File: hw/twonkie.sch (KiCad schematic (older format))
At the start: 55 parts, among them J1 USB4151, J2 690-024-294T331, J3 629105150521, Q1 BSD840N, Q2 BSD840N, Q3 BSD840N, SW1 EVQ-P7M01P, U1 INA260, U2 INA260, U3 MIC5504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

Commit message: Add back bootloader selection via USB_ID
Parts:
- added Q4: BSD840N, Package_TO_SOT_SMD:SOT-363_SC-70-6, symbol Transistor_FET:FDG6335N
- added R27: 35k7, Resistor_SMD:R_0402_1005Metric_Pad0.72x0.64mm_HandSolder, symbol Device:R
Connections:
- net +3V3: now also R1.1, R27.1; no longer R24.1
- net BOOT: now also R1.2, Q4.1 (S); no longer R1.1, SW1.2
- net GND: now also R24.2, Q4.6 (D); no longer R1.2
- net USB_B_ID: now reaches J3.4 (ID)
- net USB_B_ID: now also SW1.1, Q4.2 (G), R27.2
- new net: R24.1, SW1.2
- no-connect marks 7 -> 6
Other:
- note added: "Bootloader mode"
- note added: "Use A-to-A cable plugged into\nOTG adapter for bootloader mode,\nor use normal Micro-B cable and\nhold SW1 while plugging."
- moved on the sheet: R24
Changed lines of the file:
@@
-$EndComp
-$Comp
-L Switch:SW_Push SW1
-U 1 1 5FAB092D
-P 7500 3200
-F 0 "SW1" H 7500 3400 50  0000 C CNN
-F 1 "EVQ-P7M01P" H 7500 3100 50  0000 C CNN
-F 2 "Button_Switch_SMD:SW_SPST_EVQP7C" H 7500 3500 50  0001 C CNN
-F 3 "http://www.apem.com/int/index.php?controller=attachment&id_attachment=1371" H 7500 3500 50  0001 C CNN
-F 4 "P16770CT-ND" H 7500 3200 50  0001 C CNN "DigiKey P/N"
-F 5 "Panasonic" H 7500 3200 50  0001 C CNN "Manufacturer"
-F 6 "EVQ-P7M01P" H 7500 3200 50  0001 C CNN "Mfg P/N"
-	1    7500 3200
-	-1   0    0    -1
 $EndComp
 $Comp
@@
 	0    -1   -1   0
 $EndComp
-$Comp
-L power:GND #PWR0124
-U 1 1 5FE51FD2
-P 7100 4250
-F 0 "#PWR0124" H 7100 4000 50  0001 C CNN
-F 1 "GND" H 7105 4077 50  0000 C CNN
-F 2 "" H 7100 4250 50  0001 C CNN
-F 3 "" H 7100 4250 50  0001 C CNN
-	1    7100 4250
-	-1   0    0    -1
-$EndComp
-Wire Wire Line
-	7100 3950 8400 3950
-Wire Wire Line
-	7300 3200 7100 3200
-$Comp
-L power:+3V3 #PWR0125
-U 1 1 5FE52452
-P 7850 2900
-F 0 "#PWR0125" H 7850 2750 50  0001 C CNN
-F 1 "+3V3" H 7865 3073 50  0000 C CNN
-F 2 "" H 7850 2900 50  0001 C CNN
-F 3 "" H 7850 2900 50  0001 C CNN
-	1    7850 2900
-	1    0    0    -1
-$EndComp
-$Comp
-L Device:R R1
-U 1 1 5FE52997
-P 7100 4100
-F 0 "R1" H 7170 4146 50  0000 L CNN
-F 1 "35k7" H 7170 4055 50  0000 L CNN
-F 2 "Resistor_SMD:R_0402_1005Metric_Pad0.72x0.64mm_HandSolder" V 7030 4100 50  0001 C CNN
-F 3 "~" H 7100 4100 50  0001 C CNN
-F 4 "311-35.7KLRCT-ND" H 7100 4100 50  0001 C CNN "DigiKey P/N"
-F 5 "RC0402FR-0735K7L" H 7100 4100 50  0001 C CNN "Mfg P/N"
-F 6 "Yageo" H 7100 4100 50  0001 C CNN "Manufacturer"
-	1    7100 4100
-	1    0    0    -1
-$EndComp
 Wire Wire Line
 	8400 4350 7500 4350
@@
 	0    1    1    0
 $EndComp
-Wire Wire Line
-	7100 3950 7100 3200
 $Comp
 L Device:R R22
@@
 $EndComp
 NoConn ~ 10500 4950
-NoConn ~ 4600 7300
 $Comp
 L power:PWR_FLAG #FLG0101
@@
 NoConn ~ 7500 4550
 NoConn ~ 7500 4650
-Wire Wire Line
-	7700 3200 7850 3200
 NoConn ~ 7500 3750
 NoConn ~ 7500 3850
@@
 Wire Wire Line
 	9100 3250 9700 3250
-Connection ~ 7100 3950
-$Comp
-L Device:R R24
-U 1 1 5FB6691F
-P 7850 3050
-F 0 "R24" H 7920 3096 50  0000 L CNN
-F 1 "100" H 7920 3005 50  0000 L CNN
-F 2 "Resistor_SMD:R_0402_1005Metric_Pad0.72x0.64mm_HandSolder" V 7780 3050 50  0001 C CNN
-F 3 "~" H 7850 3050 50  0001 C CNN
-F 4 "RC0402FR-07100RL" H 7850 3050 50  0001 C CNN "Mfg P/N"
-F 5 "Yageo" H 7850 3050 50  0001 C CNN "Manufacturer"
-	1    7850 3050
-	1    0    0    -1
-$EndComp
 $Comp
 L Device:R R25
@@
 Wire Wire Line
 	7100 5250 8400 5250
+Wire Wire Line
+	7500 3950 8400 3950
+Wire Wire Line
+	4600 7300 4950 7300
+Text Label 4950 7300 2    50   ~ 0
+USB_B_ID
+Wire Notes Line
+	5600 5150 5600 2550
+Wire Notes Line
+	5600 5150 6950 5150
+Text Notes 5650 3050 0    39   ~ 0
+Use A-to-A cable plugged into\nOTG adapter for bootloader mode,\nor use normal Micro-B cable and\nhold SW1 while plugging.
+Text Notes 6900 2750 2    98   ~ 0
+Bootloader mode
+Text Label 6850 3800 2    50   ~ 0
+BOOT
+Wire Wire Line
+	6400 3800 6850 3800
+Text Label 5700 4000 0    50   ~ 0
+USB_B_ID
+$Comp
+L power:GND #PWR05
+U 1 1 5FF50DC2
+P 6400 4900
+F 0 "#PWR05" H 6400 4650 50  0001 C CNN
+F 1 "GND" H 6405 4727 50  0000 C CNN
+F 2 "" H 6400 4900 50  0001 C CNN
+F 3 "" H 6400 4900 50  0001 C CNN
+	1    6400 4900
+	-1   0    0    -1
+$EndComp
+$Comp
+L power:+3V3 #PWR04
+U 1 1 5FF50DC8
+P 6100 3300
+F 0 "#PWR04" H 6100 3150 50  0001 C CNN
+F 1 "+3V3" H 6115 3473 50  0000 C CNN
+F 2 "" H 6100 3300 50  0001 C CNN
+F 3 "" H 6100 3300 50  0001 C CNN
+	1    6100 3300
+	1    0    0    -1
+$EndComp
+$Comp
+L Device:R R27
+U 1 1 5FF50DD1
+P 6100 3550
+F 0 "R27" H 6170 3596 50  0000 L CNN
+F 1 "35k7" H 6170 3505 50  0000 L CNN
+F 2 "Resistor_SMD:R_0402_1005Metric_Pad0.72x0.64mm_HandSolder" V 6030 3550 50  0001 C CNN
+F 3 "~" H 6100 3550 50  0001 C CNN
+F 4 "311-35.7KLRCT-ND" H 6100 3550 50  0001 C CNN "DigiKey P/N"
+F 5 "RC0402FR-0735K7L" H 6100 3550 50  0001 C CNN "Mfg P/N"
+F 6 "Yageo" H 6100 3550 50  0001 C CNN "Manufacturer"
+	1    6100 3550
+	1    0    0    -1
+$EndComp
+$Comp
+L Transistor_FET:FDG6335N Q4
+U 1 1 5FF50DE2
+P 6300 4000
+F 0 "Q4" H 6505 4046 50  0000 L CNN
+F 1 "BSD840N" H 6505 3955 50  0000 L CNN
+F 2 "Package_TO_SOT_SMD:SOT-363_SC-70-6" H 6500 3925 50  0001 L CIN
+F 3 "http://www.gneic.com/product/datasheet/FDG6335N-1122853.pdf" H 6300 4000 50  0001 L CNN
+F 4 "BSD840NH6327XTSA1CT-ND" H 6300 4000 50  0001 C CNN "DigiKey P/N"
+F 5 "Infineon" H 6300 4000 50  0001 C CNN "Manufacturer"
+F 6 "BSD840NH6327XTSA1" H 6300 4000 50  0001 C CNN "Mfg P/N"
+	1    6300 4000
+	1    0    0    1
+$EndComp
+Wire Wire Line
+	6100 3300 6100 3400
+Wire Wire Line
+	6100 3400 6400 3400
+Connection ~ 6100 3400
+Wire Wire Line
+	6100 3700 6100 4000
+Wire Wire Line
+	6100 4000 6100 4100
+Connection ~ 6100 4000
+Wire Wire Line
+	6100 4500 6100 4600
+Wire Wire Line
+	6100 4900 6400 4900
+Wire Wire Line
+	6400 4900 6400 4200
+Connection ~ 6400 4900
+Wire Wire Line
+	6100 4000 5700 4000
+Wire Wire Line
+	6400 3700 6400 3800
+Connection ~ 6400 3800
+$Comp
+L Switch:SW_Push SW1
+U 1 1 5FF46D11
+P 6100 4300
+F 0 "SW1" H 6100 4500 50  0000 C CNN
+F 1 "EVQ-P7M01P" H 6100 4200 50  0000 C CNN
+F 2 "Button_Switch_SMD:SW_SPST_EVQP7C" H 6100 4600 50  0001 C CNN
+F 3 "http://www.apem.com/int/index.php?controller=attachment&id_attachment=1371" H 6100 4600 50  0001 C CNN
+F 4 "P16770CT-ND" H 6100 4300 50  0001 C CNN "DigiKey P/N"
+F 5 "Panasonic" H 6100 4300 50  0001 C CNN "Manufacturer"
+F 6 "EVQ-P7M01P" H 6100 4300 50  0001 C CNN "Mfg P/N"
+	1    6100 4300
+	0    -1   1    0
+$EndComp
+$Comp
+L Device:R R24
+U 1 1 5FB6691F
+P 6100 4750
+F 0 "R24" H 6170 4796 50  0000 L CNN
+F 1 "100" H 6170 4705 50  0000 L CNN
+F 2 "Resistor_SMD:R_0402_1005Metric_Pad0.72x0.64mm_HandSolder" V 6030 4750 50  0001 C CNN
+F 3 "~" H 6100 4750 50  0001 C CNN
+F 4 "RC0402FR-07100RL" H 6100 4750 50  0001 C CNN "Mfg P/N"
+F 5 "Yageo" H 6100 4750 50  0001 C CNN "Manufacturer"
+	1    6100 4750
+	1    0    0    -1
+$EndComp
+$Comp
+L Device:R R1
+U 1 1 5FF46D15
+P 6400 3550
+F 0 "R1" H 6470 3596 50  0000 L CNN
+F 1 "35k7" H 6470 3505 50  0000 L CNN
+F 2 "Resistor_SMD:R_0402_1005Metric_Pad0.72x0.64mm_HandSolder" V 6330 3550 50  0001 C CNN
+F 3 "~" H 6400 3550 50  0001 C CNN
+F 4 "311-35.7KLRCT-ND" H 6400 3550 50  0001 C CNN "DigiKey P/N"
+F 5 "RC0402FR-0735K7L" H 6400 3550 50  0001 C CNN "Mfg P/N"
+F 6 "Yageo" H 6400 3550 50  0001 C CNN "Manufacturer"
+	1    6400 3550
+	1    0    0    -1
+$EndComp
 $EndSCHEMATC

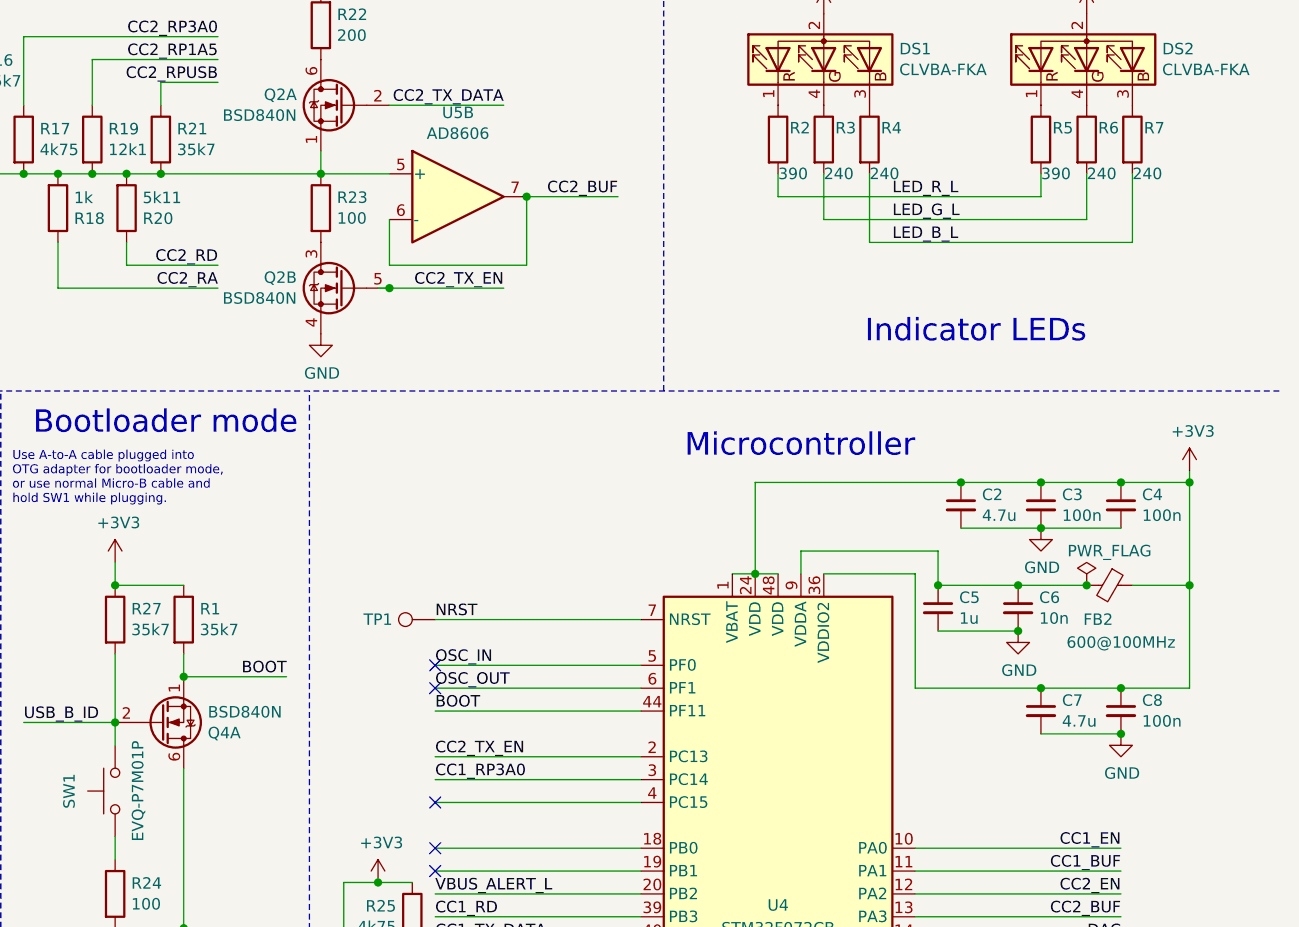
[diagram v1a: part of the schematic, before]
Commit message: Last minute fixes
 * Add back C8 which had accidentally been deleted
 * Flip Q4 source<->drain
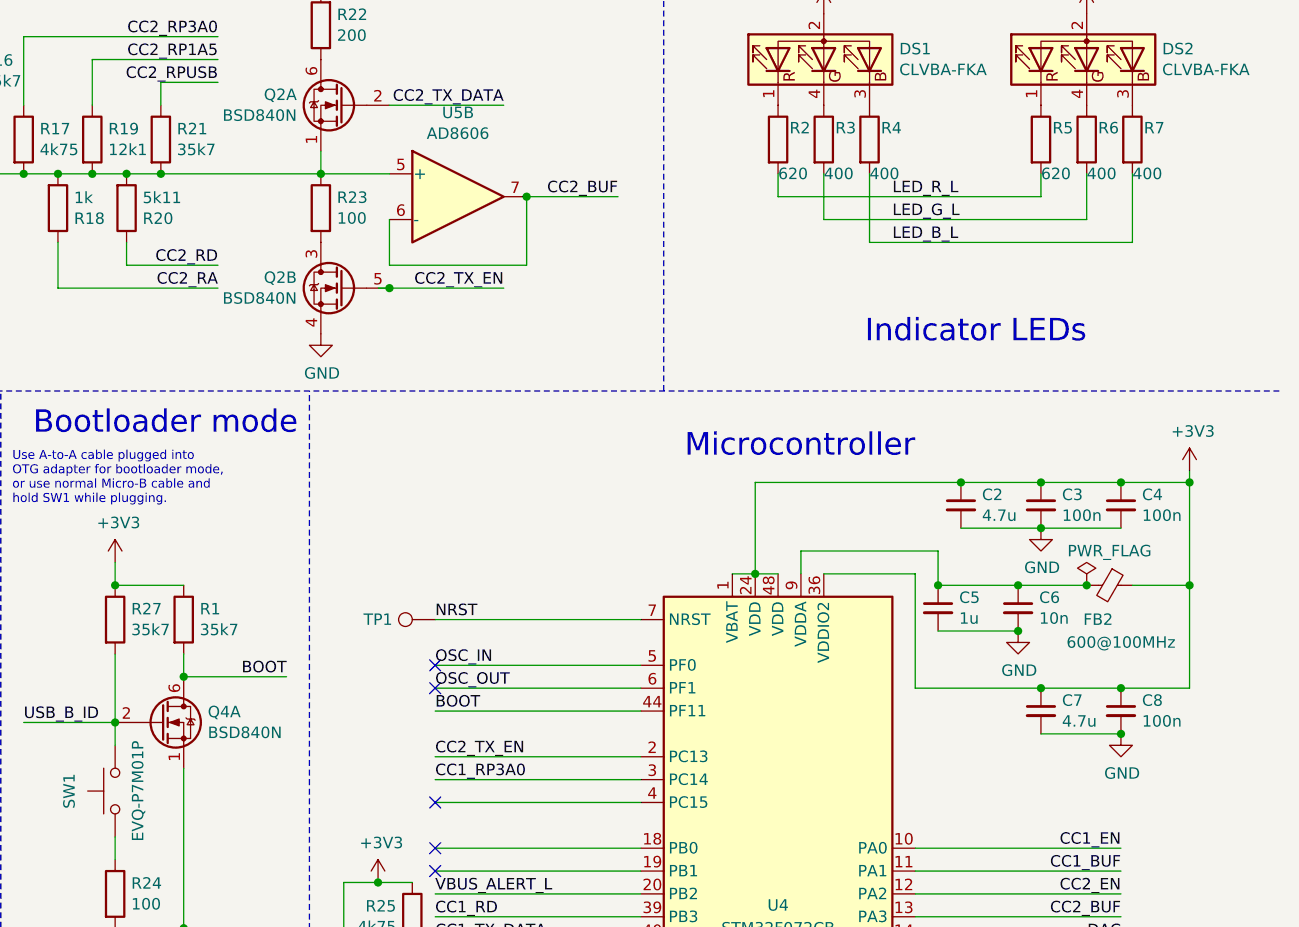
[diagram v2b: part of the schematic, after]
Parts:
- J3: footprint Connector_USB:USB_Micro-B_Wuerth_629105150521 -> twonkie:USB_Micro-B_Wuerth_629105150521_HandSolder
- R1, R13, R16, R21, R27, R8: DigiKey P/N 311-35.7KLRCT-ND -> (none)
- R17, R25, R26, R9: DigiKey P/N 311-4.75KLCT-ND -> (none)
- R2, R5: value 390 -> 620; DigiKey P/N YAG3239CT-ND -> (none); Mfg P/N RC0402FR-07806RL -> RC0402FR-07620RL
- R3, R4, R6, R7: value 240 -> 400; Mfg P/N RC0402FR-07240RL -> RC0402FR-07402RL
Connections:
- net BOOT: now also Q4.6 (D); no longer Q4.1 (S)
- net GND: now also Q4.1 (S); no longer Q4.6 (D)
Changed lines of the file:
@@
 F 0 "J3" H 4357 7567 50  0000 C CNN
 F 1 "629105150521" H 4357 7476 50  0000 C CNN
-F 2 "Connector_USB:USB_Micro-B_Wuerth_629105150521" H 4450 7050 50  0001 C CNN
+F 2 "twonkie:USB_Micro-B_Wuerth_629105150521_HandSolder" H 4450 7050 50  0001 C CNN
 F 3 "~" H 4450 7050 50  0001 C CNN
 F 4 "732-5960-1-ND" H 4300 7100 50  0001 C CNN "DigiKey P/N"
@@
 P 9000 1450
 F 0 "R2" H 9050 1500 50  0000 L CNN
-F 1 "390" H 9000 1300 50  0000 L CNN
+F 1 "620" H 9000 1300 50  0000 L CNN
 F 2 "Resistor_SMD:R_0402_1005Metric_Pad0.72x0.64mm_HandSolder" V 8930 1450 50  0001 C CNN
 F 3 "~" H 9000 1450 50  0001 C CNN
-F 4 "YAG3239CT-ND" H 9000 1450 50  0001 C CNN "DigiKey P/N"
-F 5 "RC0402FR-07806RL" H 9000 1450 50  0001 C CNN "Mfg P/N"
+F 4 "" H 9000 1450 50  0001 C CNN "DigiKey P/N"
+F 5 "RC0402FR-07620RL" H 9000 1450 50  0001 C CNN "Mfg P/N"
 F 6 "Yageo" H 9000 1450 50  0001 C CNN "Manufacturer"
 	1    9000 1450
@@
 P 9200 1450
 F 0 "R3" H 9250 1500 50  0000 L CNN
-F 1 "240" H 9200 1300 50  0000 L CNN
+F 1 "400" H 9200 1300 50  0000 L CNN
 F 2 "Resistor_SMD:R_0402_1005Metric_Pad0.72x0.64mm_HandSolder" V 9130 1450 50  0001 C CNN
 F 3 "~" H 9200 1450 50  0001 C CNN
 F 4 "" H 9200 1450 50  0001 C CNN "DigiKey P/N"
-F 5 "RC0402FR-07240RL" H 9200 1450 50  0001 C CNN "Mfg P/N"
+F 5 "RC0402FR-07402RL" H 9200 1450 50  0001 C CNN "Mfg P/N"
 F 6 "Yageo" H 9200 1450 50  0001 C CNN "Manufacturer"
 	1    9200 1450
@@
 P 9400 1450
 F 0 "R4" H 9450 1500 50  0000 L CNN
-F 1 "240" H 9400 1300 50  0000 L CNN
+F 1 "400" H 9400 1300 50  0000 L CNN
 F 2 "Resistor_SMD:R_0402_1005Metric_Pad0.72x0.64mm_HandSolder" V 9330 1450 50  0001 C CNN
 F 3 "~" H 9400 1450 50  0001 C CNN
 F 4 "" H 9400 1450 50  0001 C CNN "DigiKey P/N"
-F 5 "RC0402FR-07240RL" H 9400 1450 50  0001 C CNN "Mfg P/N"
+F 5 "RC0402FR-07402RL" H 9400 1450 50  0001 C CNN "Mfg P/N"
 F 6 "Yageo" H 9400 1450 50  0001 C CNN "Manufacturer"
 	1    9400 1450
@@
 P 10150 1450
 F 0 "R5" H 10200 1500 50  0000 L CNN
-F 1 "390" H 10150 1300 50  0000 L CNN
+F 1 "620" H 10150 1300 50  0000 L CNN
 F 2 "Resistor_SMD:R_0402_1005Metric_Pad0.72x0.64mm_HandSolder" V 10080 1450 50  0001 C CNN
 F 3 "~" H 10150 1450 50  0001 C CNN
-F 4 "YAG3239CT-ND" H 10150 1450 50  0001 C CNN "DigiKey P/N"
-F 5 "RC0402FR-07806RL" H 10150 1450 50  0001 C CNN "Mfg P/N"
+F 4 "" H 10150 1450 50  0001 C CNN "DigiKey P/N"
+F 5 "RC0402FR-07620RL" H 10150 1450 50  0001 C CNN "Mfg P/N"
 F 6 "Yageo" H 10150 1450 50  0001 C CNN "Manufacturer"
 	1    10150 1450
@@
 P 10350 1450
 F 0 "R6" H 10400 1500 50  0000 L CNN
-F 1 "240" H 10350 1300 50  0000 L CNN
+F 1 "400" H 10350 1300 50  0000 L CNN
 F 2 "Resistor_SMD:R_0402_1005Metric_Pad0.72x0.64mm_HandSolder" V 10280 1450 50  0001 C CNN
 F 3 "~" H 10350 1450 50  0001 C CNN
 F 4 "" H 10350 1450 50  0001 C CNN "DigiKey P/N"
-F 5 "RC0402FR-07240RL" H 10350 1450 50  0001 C CNN "Mfg P/N"
+F 5 "RC0402FR-07402RL" H 10350 1450 50  0001 C CNN "Mfg P/N"
 F 6 "Yageo" H 10350 1450 50  0001 C CNN "Manufacturer"
 	1    10350 1450
@@
 P 10550 1450
 F 0 "R7" H 10600 1500 50  0000 L CNN
-F 1 "240" H 10550 1300 50  0000 L CNN
+F 1 "400" H 10550 1300 50  0000 L CNN
 F 2 "Resistor_SMD:R_0402_1005Metric_Pad0.72x0.64mm_HandSolder" V 10480 1450 50  0001 C CNN
 F 3 "~" H 10550 1450 50  0001 C CNN
 F 4 "" H 10550 1450 50  0001 C CNN "DigiKey P/N"
-F 5 "RC0402FR-07240RL" H 10550 1450 50  0001 C CNN "Mfg P/N"
+F 5 "RC0402FR-07402RL" H 10550 1450 50  0001 C CNN "Mfg P/N"
 F 6 "Yageo" H 10550 1450 50  0001 C CNN "Manufacturer"
 	1    10550 1450
@@
 F 2 "Resistor_SMD:R_0402_1005Metric_Pad0.72x0.64mm_HandSolder" V 5380 1150 50  0001 C CNN
 F 3 "~" H 5450 1150 50  0001 C CNN
-F 4 "311-35.7KLRCT-ND" H 5450 1150 50  0001 C CNN "DigiKey P/N"
+F 4 "" H 5450 1150 50  0001 C CNN "DigiKey P/N"
 F 5 "RC0402FR-0735K7L" H 5450 1150 50  0001 C CNN "Mfg P/N"
 F 6 "Yageo" H 5450 1150 50  0001 C CNN "Manufacturer"
@@
 F 2 "Resistor_SMD:R_0402_1005Metric_Pad0.72x0.64mm_HandSolder" V 5630 1450 50  0001 C CNN
 F 3 "~" H 5700 1450 50  0001 C CNN
-F 4 "311-4.75KLCT-ND" H 5700 1450 50  0001 C CNN "DigiKey P/N"
+F 4 "" H 5700 1450 50  0001 C CNN "DigiKey P/N"
 F 5 "RC0402FR-074K75L" H 5700 1450 50  0001 C CNN "Mfg P/N"
 F 6 "Yageo" H 5700 1450 50  0001 C CNN "Manufacturer"
@@
 F 4 "RC0402FR-0735K7L" H 6300 1450 50  0001 C CNN "Mfg P/N"
 F 5 "Yageo" H 6300 1450 50  0001 C CNN "Manufacturer"
-F 6 "311-35.7KLRCT-ND" H 6300 1450 50  0001 C CNN "DigiKey P/N"
+F 6 "" H 6300 1450 50  0001 C CNN "DigiKey P/N"
 	1    6300 1450
 	1    0    0    -1
@@
 F 4 "RC0402FR-0735K7L" H 2400 1450 50  0001 C CNN "Mfg P/N"
 F 5 "Yageo" H 2400 1450 50  0001 C CNN "Manufacturer"
-F 6 "311-35.7KLRCT-ND" H 2400 1450 50  0001 C CNN "DigiKey P/N"
+F 6 "" H 2400 1450 50  0001 C CNN "DigiKey P/N"
 	1    2400 1450
 	1    0    0    -1
@@
 F 2 "Resistor_SMD:R_0402_1005Metric_Pad0.72x0.64mm_HandSolder" V 1730 1450 50  0001 C CNN
 F 3 "~" H 1800 1450 50  0001 C CNN
-F 4 "311-4.75KLCT-ND" H 1800 1450 50  0001 C CNN "DigiKey P/N"
+F 4 "" H 1800 1450 50  0001 C CNN "DigiKey P/N"
 F 5 "RC0402FR-074K75L" H 1800 1450 50  0001 C CNN "Mfg P/N"
 F 6 "Yageo" H 1800 1450 50  0001 C CNN "Manufacturer"
@@
 F 2 "Resistor_SMD:R_0402_1005Metric_Pad0.72x0.64mm_HandSolder" V 1480 1150 50  0001 C CNN
 F 3 "~" H 1550 1150 50  0001 C CNN
-F 4 "311-35.7KLRCT-ND" H 1550 1150 50  0001 C CNN "DigiKey P/N"
+F 4 "" H 1550 1150 50  0001 C CNN "DigiKey P/N"
 F 5 "RC0402FR-0735K7L" H 1550 1150 50  0001 C CNN "Mfg P/N"
 F 6 "Yageo" H 1550 1150 50  0001 C CNN "Manufacturer"
@@
 F 2 "Resistor_SMD:R_0402_1005Metric_Pad0.72x0.64mm_HandSolder" V 7330 4850 50  0001 C CNN
 F 3 "~" H 7400 4850 50  0001 C CNN
-F 4 "311-4.75KLCT-ND" H 7400 4850 50  0001 C CNN "DigiKey P/N"
+F 4 "" H 7400 4850 50  0001 C CNN "DigiKey P/N"
 F 5 "RC0402FR-074K75L" H 7400 4850 50  0001 C CNN "Mfg P/N"
 F 6 "Yageo" H 7400 4850 50  0001 C CNN "Manufacturer"
@@
 F 2 "Resistor_SMD:R_0402_1005Metric_Pad0.72x0.64mm_HandSolder" V 7030 5100 50  0001 C CNN
 F 3 "~" H 7100 5100 50  0001 C CNN
-F 4 "311-4.75KLCT-ND" H 7100 5100 50  0001 C CNN "DigiKey P/N"
+F 4 "" H 7100 5100 50  0001 C CNN "DigiKey P/N"
 F 5 "RC0402FR-074K75L" H 7100 5100 50  0001 C CNN "Mfg P/N"
 F 6 "Yageo" H 7100 5100 50  0001 C CNN "Manufacturer"
@@
 F 2 "Resistor_SMD:R_0402_1005Metric_Pad0.72x0.64mm_HandSolder" V 6030 3550 50  0001 C CNN
 F 3 "~" H 6100 3550 50  0001 C CNN
-F 4 "311-35.7KLRCT-ND" H 6100 3550 50  0001 C CNN "DigiKey P/N"
+F 4 "" H 6100 3550 50  0001 C CNN "DigiKey P/N"
 F 5 "RC0402FR-0735K7L" H 6100 3550 50  0001 C CNN "Mfg P/N"
 F 6 "Yageo" H 6100 3550 50  0001 C CNN "Manufacturer"
@@
 F 6 "BSD840NH6327XTSA1" H 6300 4000 50  0001 C CNN "Mfg P/N"
 	1    6300 4000
-	1    0    0    1
+	1    0    0    -1
 $EndComp
 Wire Wire Line
@@
 F 2 "Resistor_SMD:R_0402_1005Metric_Pad0.72x0.64mm_HandSolder" V 6330 3550 50  0001 C CNN
 F 3 "~" H 6400 3550 50  0001 C CNN
-F 4 "311-35.7KLRCT-ND" H 6400 3550 50  0001 C CNN "DigiKey P/N"
+F 4 "" H 6400 3550 50  0001 C CNN "DigiKey P/N"
 F 5 "RC0402FR-0735K7L" H 6400 3550 50  0001 C CNN "Mfg P/N"
 F 6 "Yageo" H 6400 3550 50  0001 C CNN "Manufacturer"

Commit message: hw: Fix ambiguous U4 part numbers
U4 still had plenty of references to the F042 that was originally
designed in there, with only the value field indicating the correct
F072. Update all fields to correctly point to the F072 part.

Fixes #3.
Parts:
- U4: symbol MCU_ST_STM32F0:STM32F042C6Tx -> MCU_ST_STM32F0:STM32F072CBTx; DigiKey P/N 497-19319-1-ND -> 497-18747-1-ND; Mfg P/N STM32F042C6T6TR -> STM32F072CBT
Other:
- note added: "Dual footprint, will accomodate\nSTM32F072CBT (TQFP48) or\nSTM32F072CBU (QFN48)"
- moved on the sheet: C2, C3, C4, C5, C6, C7, C8, FB2, TP1, TP2, TP3, U4
